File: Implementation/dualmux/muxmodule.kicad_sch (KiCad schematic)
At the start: 12 parts, among them U2 74HC00, U3 74HC00, U4 74HC00, U5 74HC00, U6 74HC00, U7 74HC00

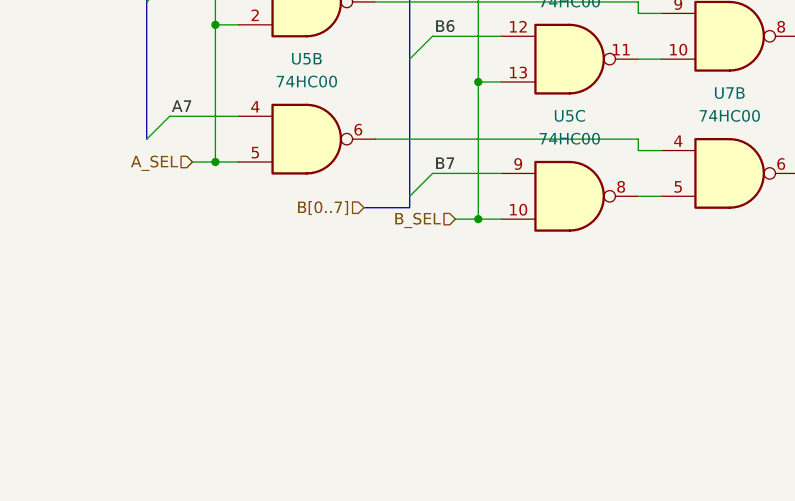
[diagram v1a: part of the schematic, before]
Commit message: Most of mux routing
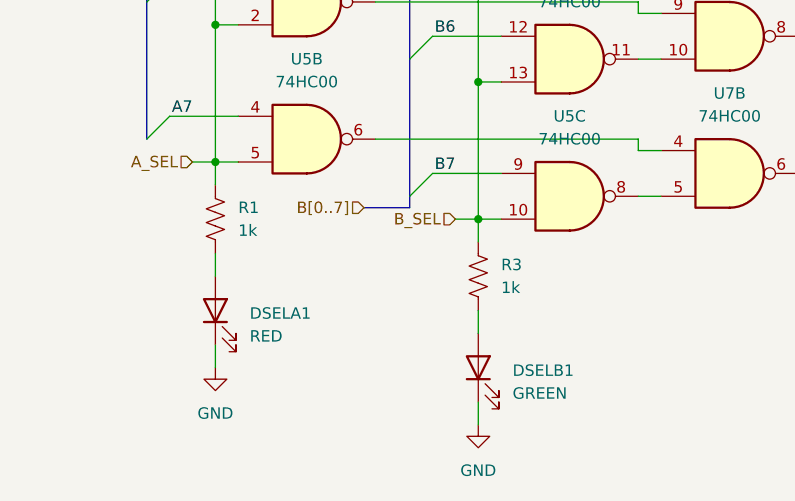
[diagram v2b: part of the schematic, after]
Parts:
- added DSELA1: RED, LED_THT:LED_D5.0mm, symbol Device:LED
- added DSELB1: GREEN, LED_THT:LED_D5.0mm, symbol Device:LED
- added R1, R3: 1k, Resistor_THT:R_Axial_DIN0207_L6.3mm_D2.5mm_P10.16mm_Horizontal, symbol Device:R_US
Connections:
- net A_SEL: now also R1.1
- net B_SEL: now also R3.1
- net GND: now also DSELA1.1 (K), DSELB1.1 (K)
- new net: DSELB1.2 (A), R3.2
- new net: DSELA1.2 (A), R1.2

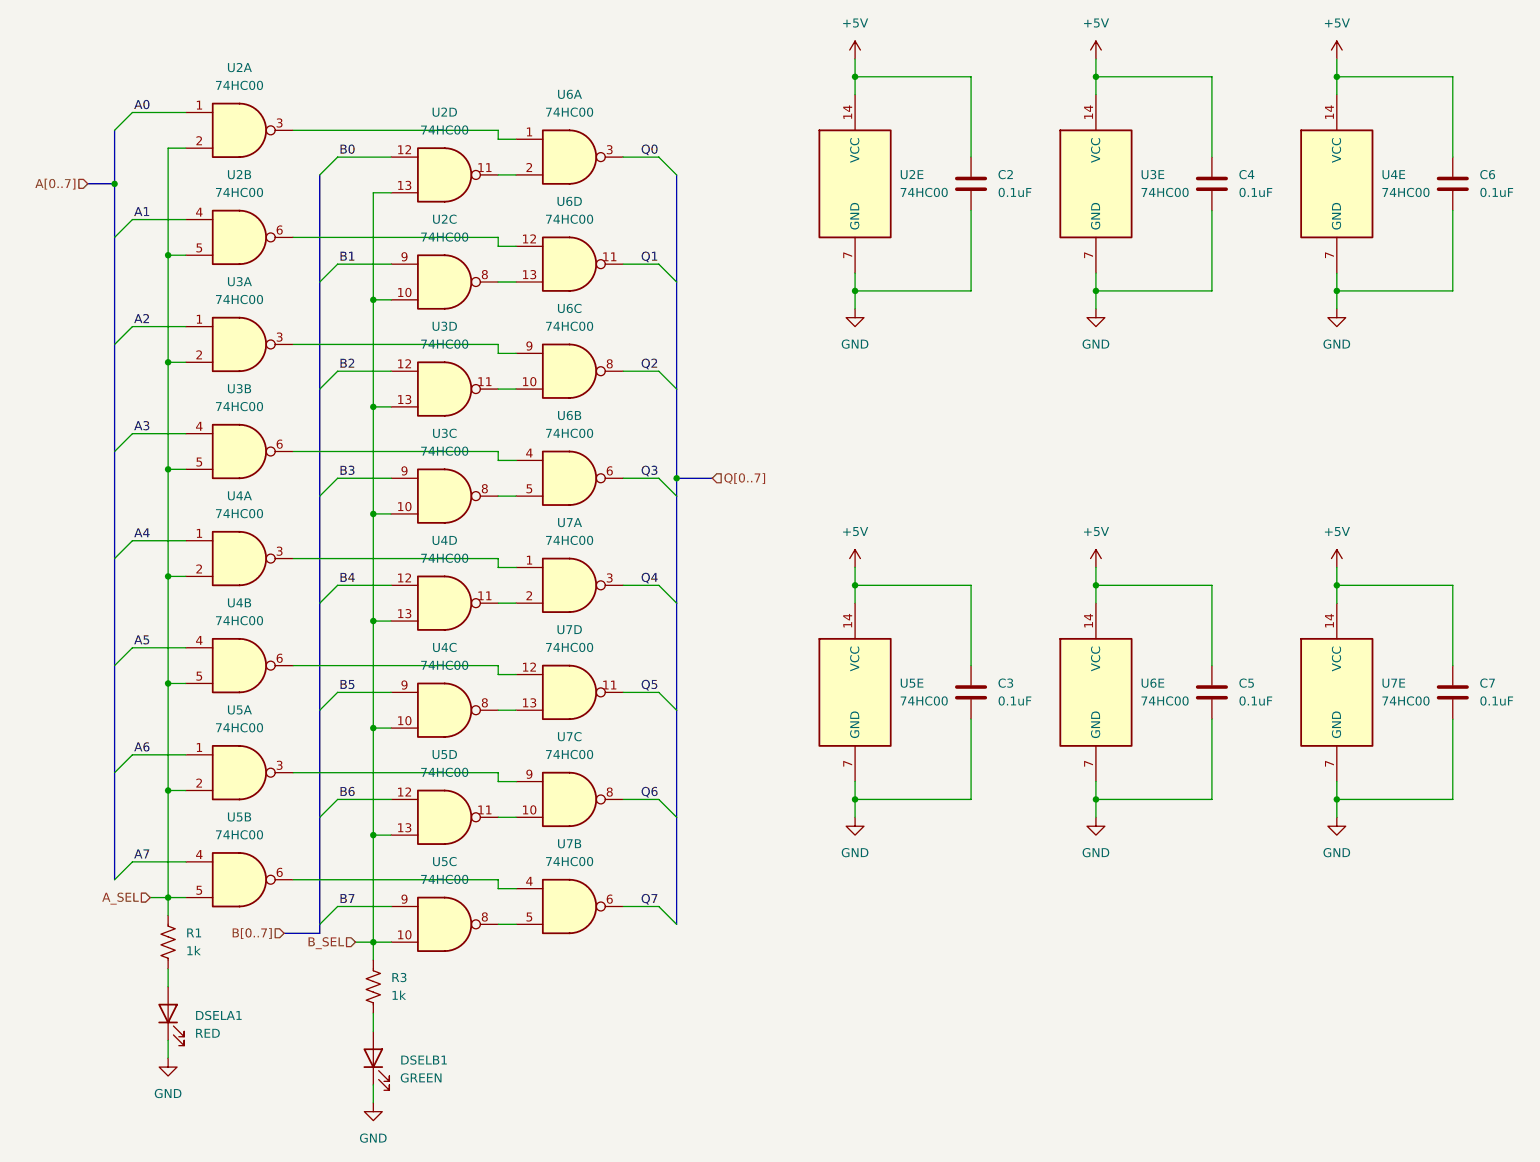
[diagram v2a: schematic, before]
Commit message: Routed 16C550 serial card
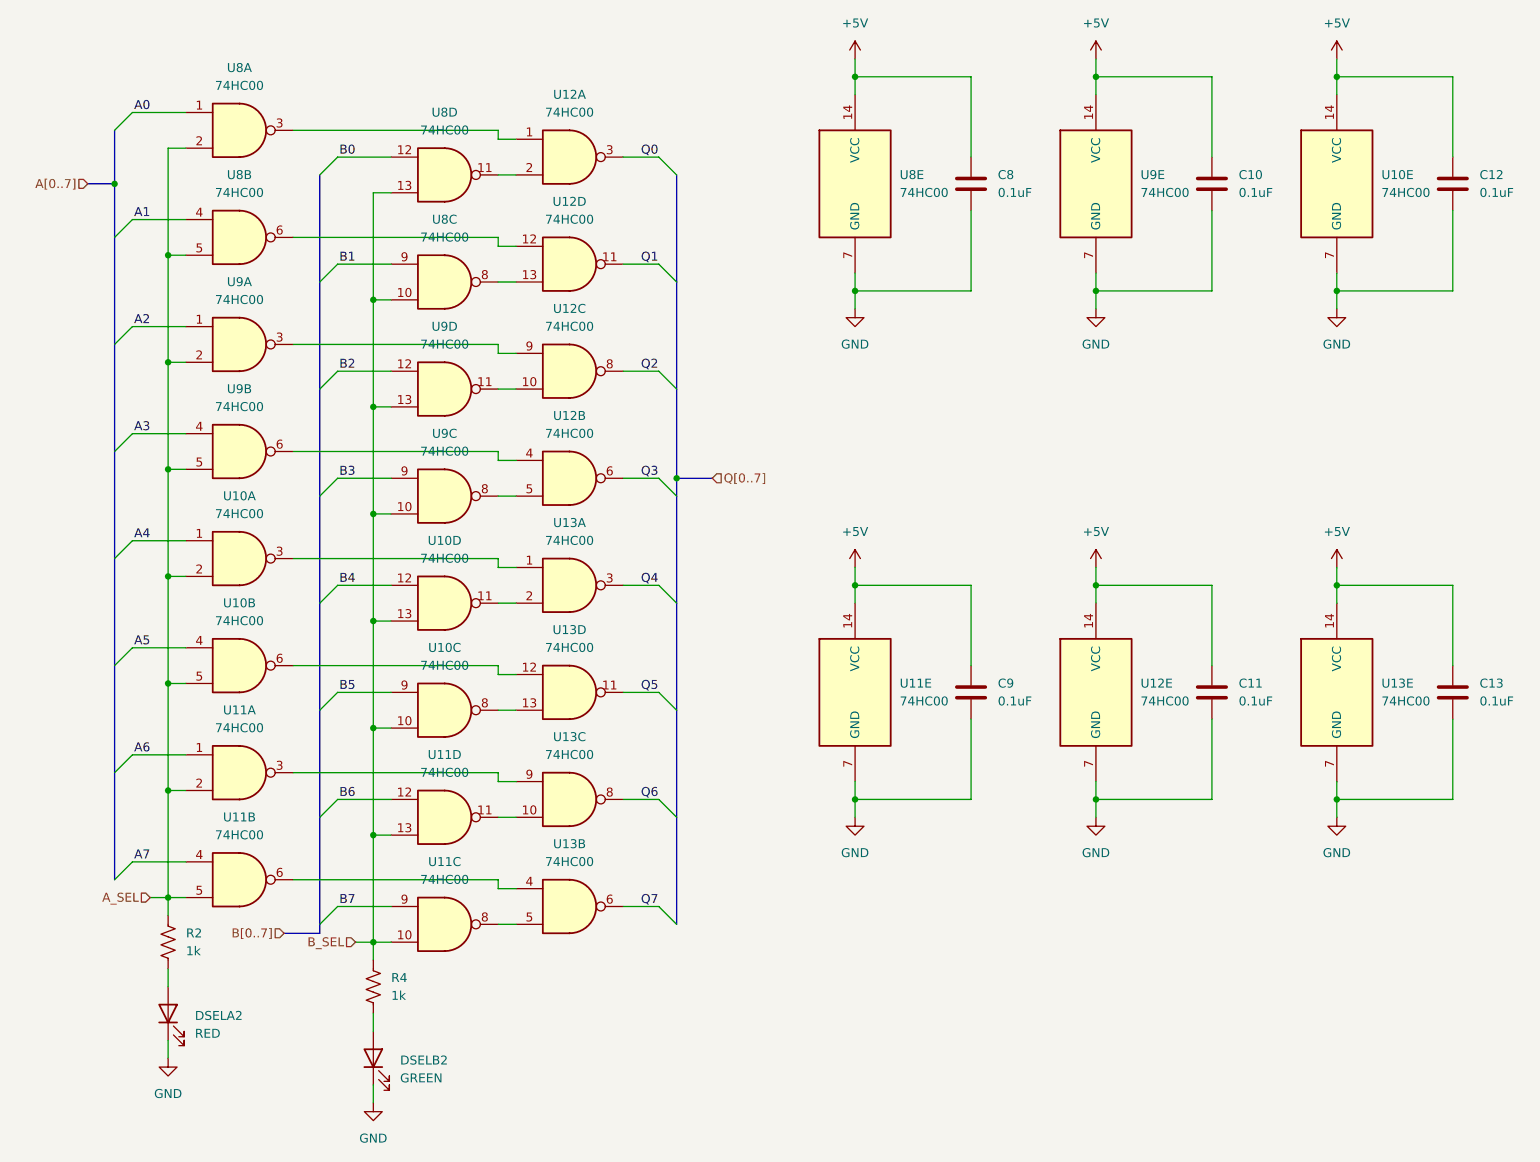
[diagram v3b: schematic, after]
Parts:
- renumbered C4 to C10, C5 to C11, C6 to C12, C7 to C13, C2 to C8, C3 to C9, DSELA1 to DSELA2, DSELB1 to DSELB2, R1 to R2, R3 to R4, U4 to U10, U5 to U11, U6 to U12, U7 to U13, U2 to U8, U3 to U9
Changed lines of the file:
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@@
 		(dnp no)
 		(fields_autoplaced yes)
-		(property "Reference" "U7"
+		(property "Reference" "U13"
 			(at 120.6417 137.16 0)
 			(effects
@@
 		(dnp no)
 		(fields_autoplaced yes)
-		(property "Reference" "U2"
+		(property "Reference" "U8"
 			(at 102.8617 48.26 0)
 			(effects
@@
 		(dnp no)
 		(fields_autoplaced yes)
-		(property "Reference" "#PWR035"
+		(property "Reference" "#PWR036"
 			(at 92.71 180.34 0)
 			(effects
@@
 		(dnp no)
 		(fields_autoplaced yes)
-		(property "Reference" "U2"
+		(property "Reference" "U8"
 			(at 73.6517 26.67 0)
 			(effects
@@
 		(dnp no)
 		(fields_autoplaced yes)
-		(property "Reference" "C2"
+		(property "Reference" "C8"
 			(at 181.61 41.9099 0)
 			(effects
@@
 		(dnp no)
 		(fields_autoplaced yes)
-		(property "Reference" "#PWR013"
+		(property "Reference" "#PWR025"
 			(at 195.58 101.6 0)
 			(effects
@@
 		(dnp no)
 		(fields_autoplaced yes)
-		(property "Reference" "U4"
+		(property "Reference" "U10"
 			(at 102.8617 109.22 0)
 			(effects
@@
 		(dnp no)
 		(fields_autoplaced yes)
-		(property "Reference" "#PWR015"
+		(property "Reference" "#PWR027"
 			(at 229.87 29.21 0)
 			(effects
@@
 		(dnp no)
 		(fields_autoplaced yes)
-		(property "Reference" "U7"
+		(property "Reference" "U13"
 			(at 120.6417 121.92 0)
 			(effects
@@
 		(dnp no)
 		(fields_autoplaced yes)
-		(property "Reference" "U2"
+		(property "Reference" "U8"
 			(at 102.8617 33.02 0)
 			(effects
@@
 		(dnp no)
 		(fields_autoplaced yes)
-		(property "Reference" "#PWR017"
+		(property "Reference" "#PWR029"
 			(at 229.87 101.6 0)
 			(effects
@@
 		(dnp no)
 		(fields_autoplaced yes)
-		(property "Reference" "U5"
+		(property "Reference" "U11"
 			(at 73.6517 133.35 0)
 			(effects
@@
 		(dnp no)
 		(fields_autoplaced yes)
-		(property "Reference" "U3"
+		(property "Reference" "U9"
 			(at 73.6517 72.39 0)
 			(effects
@@
 		(dnp no)
 		(fields_autoplaced yes)
-		(property "Reference" "U5"
+		(property "Reference" "U11"
 			(at 73.6517 118.11 0)
 			(effects
@@
 		(dnp no)
 		(fields_autoplaced yes)
-		(property "Reference" "#PWR010"
+		(property "Reference" "#PWR022"
 			(at 161.29 139.7 0)
 			(effects
@@
 		(dnp no)
 		(fields_autoplaced yes)
-		(property "Reference" "U7"
+		(property "Reference" "U13"
 			(at 120.6417 106.68 0)
 			(effects
@@
 		(dnp no)
 		(fields_autoplaced yes)
-		(property "Reference" "U3"
+		(property "Reference" "U9"
 			(at 102.8617 78.74 0)
 			(effects
@@
 		(dnp no)
 		(fields_autoplaced yes)
-		(property "Reference" "U7"
+		(property "Reference" "U13"
 			(at 236.22 114.3 0)
 			(effects
@@
 		(dnp no)
 		(fields_autoplaced yes)
-		(property "Reference" "U5"
+		(property "Reference" "U11"
 			(at 167.64 114.3 0)
 			(effects
@@
 		(dnp no)
 		(fields_autoplaced yes)
-		(property "Reference" "U4"
+		(property "Reference" "U10"
 			(at 73.6517 102.87 0)
 			(effects
@@
 		(dnp no)
 		(fields_autoplaced yes)
-		(property "Reference" "DSELB1"
+		(property "Reference" "DSELB2"
 			(at 96.52 167.9574 90)
 			(effects
@@
 		(dnp no)
 		(fields_autoplaced yes)
-		(property "Reference" "#PWR016"
+		(property "Reference" "#PWR028"
 			(at 229.87 67.31 0)
 			(effects
@@
 		(dnp no)
 		(fields_autoplaced yes)
-		(property "Reference" "#PWR012"
+		(property "Reference" "#PWR024"
 			(at 195.58 67.31 0)
 			(effects
@@
 		(dnp no)
 		(fields_autoplaced yes)
-		(property "Reference" "U7"
+		(property "Reference" "U13"
 			(at 120.6417 91.44 0)
 			(effects
@@
 		(dnp no)
 		(fields_autoplaced yes)
-		(property "Reference" "U3"
+		(property "Reference" "U9"
 			(at 201.93 41.91 0)
 			(effects
@@
 		(dnp no)
 		(fields_autoplaced yes)
-		(property "Reference" "C6"
+		(property "Reference" "C12"
 			(at 250.19 41.9099 0)
 			(effects
@@
 		(dnp no)
 		(fields_autoplaced yes)
-		(property "Reference" "U6"
+		(property "Reference" "U12"
 			(at 120.6417 30.48 0)
 			(effects
@@
 		(dnp no)
 		(fields_autoplaced yes)
-		(property "Reference" "#PWR08"
+		(property "Reference" "#PWR020"
 			(at 161.29 67.31 0)
 			(effects
@@
 		(dnp no)
 		(fields_autoplaced yes)
-		(property "Reference" "U4"
+		(property "Reference" "U10"
 			(at 73.6517 87.63 0)
 			(effects
@@
 		(dnp no)
 		(fields_autoplaced yes)
-		(property "Reference" "C4"
+		(property "Reference" "C10"
 			(at 215.9 41.9099 0)
 			(effects
@@
 		(dnp no)
 		(fields_autoplaced yes)
-		(property "Reference" "U6"
+		(property "Reference" "U12"
 			(at 201.93 114.3 0)
 			(effects
@@
 		(dnp no)
 		(fields_autoplaced yes)
-		(property "Reference" "DSELA1"
+		(property "Reference" "DSELA2"
 			(at 67.31 161.6074 90)
 			(effects
@@
 		(dnp no)
 		(fields_autoplaced yes)
-		(property "Reference" "U6"
+		(property "Reference" "U12"
 			(at 120.6417 60.96 0)
 			(effects
@@
 		(dnp no)
 		(fields_autoplaced yes)
-		(property "Reference" "C3"
+		(property "Reference" "C9"
 			(at 181.61 114.2999 0)
 			(effects
@@
 		(dnp no)
 		(fields_autoplaced yes)
-		(property "Reference" "C5"
+		(property "Reference" "C11"
 			(at 215.9 114.2999 0)
 			(effects
@@
 		(dnp no)
 		(fields_autoplaced yes)
-		(property "Reference" "U2"
+		(property "Reference" "U8"
 			(at 73.6517 41.91 0)
 			(effects
@@
 		(dnp no)
 		(fields_autoplaced yes)
-		(property "Reference" "U6"
+		(property "Reference" "U12"
 			(at 120.6417 45.72 0)
 			(effects
@@
 		(dnp no)
 		(fields_autoplaced yes)
-		(property "Reference" "#PWR014"
+		(property "Reference" "#PWR026"
 			(at 195.58 139.7 0)
 			(effects
@@
 		(dnp no)
 		(fields_autoplaced yes)
-		(property "Reference" "#PWR011"
+		(property "Reference" "#PWR023"
 			(at 195.58 29.21 0)
 			(effects
@@
 		(dnp no)
 		(fields_autoplaced yes)
-		(property "Reference" "U6"
+		(property "Reference" "U12"
 			(at 120.6417 76.2 0)
 			(effects
@@
 		(dnp no)
 		(fields_autoplaced yes)
-		(property "Reference" "U3"
+		(property "Reference" "U9"
 			(at 102.8617 63.5 0)
 			(effects
@@
 		(dnp no)
 		(fields_autoplaced yes)
-		(property "Reference" "C7"
+		(property "Reference" "C13"
 			(at 250.19 114.2999 0)
 			(effects
@@
 		(dnp no)
 		(fields_autoplaced yes)
-		(property "Reference" "U5"
+		(property "Reference" "U11"
 			(at 102.8617 124.46 0)
 			(effects
@@
 		(dnp no)
 		(fields_autoplaced yes)
-		(property "Reference" "#PWR09"
+		(property "Reference" "#PWR021"
 			(at 161.29 101.6 0)
 			(effects
@@
 		(dnp no)
 		(fields_autoplaced yes)
-		(property "Reference" "#PWR033"
+		(property "Reference" "#PWR034"
 			(at 63.5 173.99 0)
 			(effects
@@
 		(dnp no)
 		(fields_autoplaced yes)
-		(property "Reference" "U4"
+		(property "Reference" "U10"
 			(at 102.8617 93.98 0)
 			(effects
@@
 		(dnp no)
 		(fields_autoplaced yes)
-		(property "Reference" "U2"
+		(property "Reference" "U8"
 			(at 167.64 41.91 0)
 			(effects
@@
 		(dnp no)
 		(fields_autoplaced yes)
-		(property "Reference" "U4"
+		(property "Reference" "U10"
 			(at 236.22 41.91 0)
 			(effects
@@
 		(dnp no)
 		(fields_autoplaced yes)
-		(property "Reference" "U3"
+		(property "Reference" "U9"
 			(at 73.6517 57.15 0)
 			(effects
@@
 		(dnp no)
 		(fields_autoplaced yes)
-		(property "Reference" "#PWR07"
+		(property "Reference" "#PWR019"
 			(at 161.29 29.21 0)
 			(effects
@@
 		(dnp no)
 		(fields_autoplaced yes)
-		(property "Reference" "R1"
+		(property "Reference" "R2"
 			(at 66.04 149.8599 0)
 			(effects
@@
 		(dnp no)
 		(fields_autoplaced yes)
-		(property "Reference" "#PWR018"
+		(property "Reference" "#PWR030"
 			(at 229.87 139.7 0)
 			(effects
@@
 		(dnp no)
 		(fields_autoplaced yes)
-		(property "Reference" "U5"
+		(property "Reference" "U11"
 			(at 102.8617 139.7 0)
 			(effects
@@
 		(dnp no)
 		(fields_autoplaced yes)
-		(property "Reference" "R3"
+		(property "Reference" "R4"
 			(at 95.25 156.2099 0)
 			(effects
